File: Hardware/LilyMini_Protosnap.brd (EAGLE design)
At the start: 77.5 x 53.3 mm, 77 parts, among them Q1 ZXMP6A13F, U1 SAMD11D14A-M, U2 AP2112K-3.3V, U3 ALS-PT19, Y1 32.768kHz

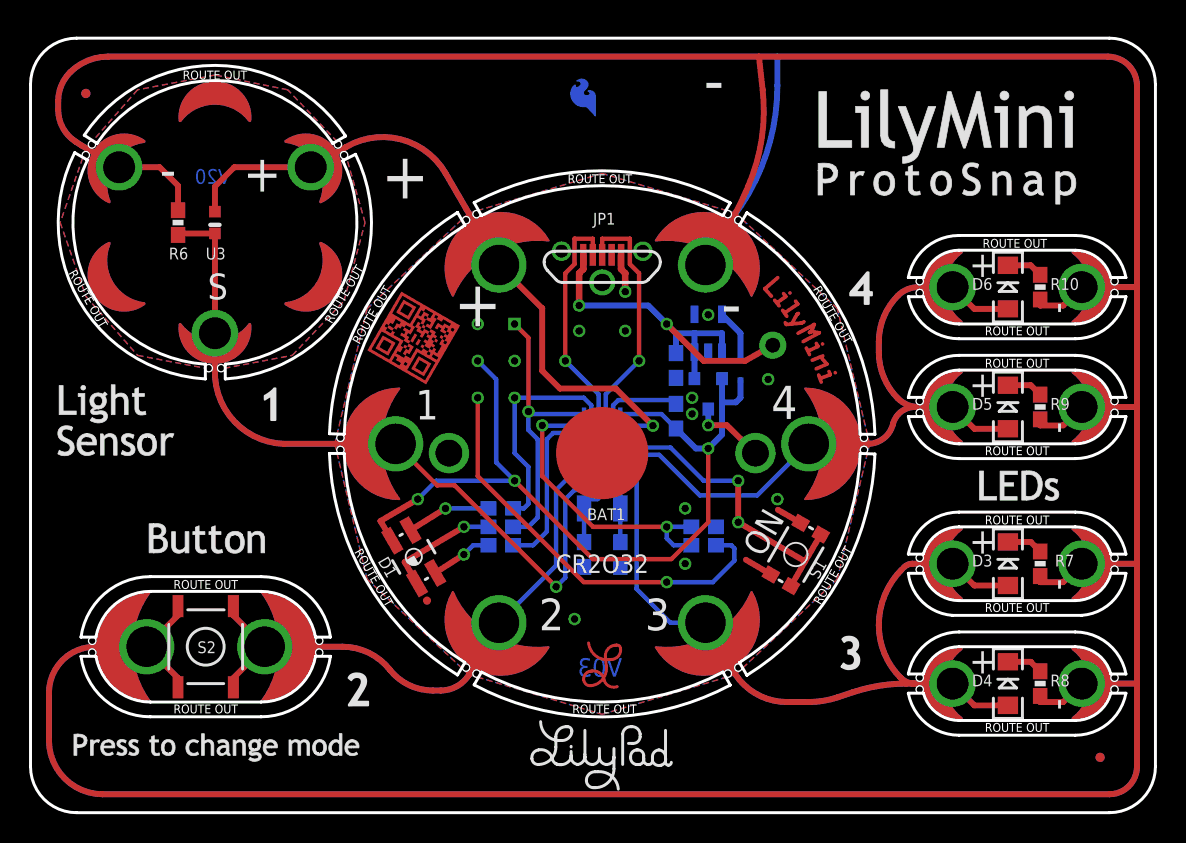
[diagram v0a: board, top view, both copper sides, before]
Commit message: Changed mouse bites from 0.02 to 0.015
Per Advanced Circuits, annular around original 0.02 drill hits would
reduce trace to hairline. Drills reduced to 0.015 to reduce this issue.
Smaller drills may make snapping harder, evaluate on proto.
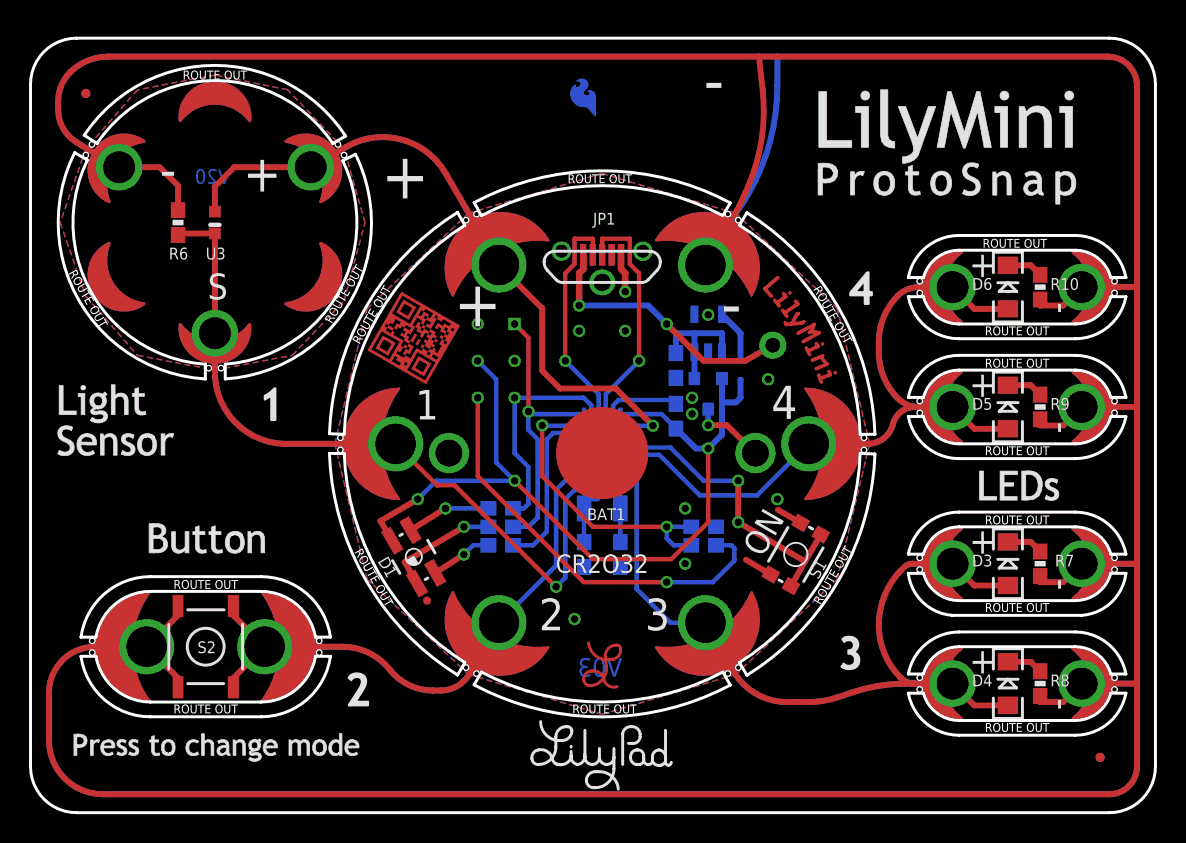
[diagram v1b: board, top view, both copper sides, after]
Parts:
- JP1: value USB_MICROB_PLUGUSB-B-MICRO-SMD-VERT -> (none)
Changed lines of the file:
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@@
 <setting verticaltext="up"/>
 </settings>
-<grid distance="0.25" unitdist="mm" unit="mm" style="lines" multiple="4" display="yes" altdistance="0.00625" altunitdist="inch" altunit="inch"/>
+<grid distance="0.0125" unitdist="inch" unit="inch" style="lines" multiple="4" display="yes" altdistance="0.00625" altunitdist="inch" altunit="inch"/>
 <layers>
 <layer number="1" name="Top" color="4" fill="1" visible="no" active="yes"/>
@@
 <layer number="42" name="bRestrict" color="1" fill="10" visible="no" active="yes"/>
 <layer number="43" name="vRestrict" color="2" fill="10" visible="no" active="yes"/>
-<layer number="44" name="Drills" color="7" fill="1" visible="no" active="yes"/>
-<layer number="45" name="Holes" color="7" fill="1" visible="no" active="yes"/>
+<layer number="44" name="Drills" color="7" fill="1" visible="yes" active="yes"/>
+<layer number="45" name="Holes" color="7" fill="1" visible="yes" active="yes"/>
 <layer number="46" name="Milling" color="3" fill="1" visible="no" active="yes"/>
 <layer number="47" name="Measures" color="7" fill="1" visible="yes" active="yes"/>
@@
 <vertex x="7.3715875" y="31.496"/>
 </polygon>
-<hole x="13.123915625" y="30.615959375" drill="0.508"/>
-<hole x="12.276084375" y="30.615959375" drill="0.508"/>
-<hole x="21.169115625" y="46.019140625" drill="0.508"/>
-<hole x="21.59303125" y="45.284896875" drill="0.508"/>
-<hole x="3.80696875" y="45.284896875" drill="0.508"/>
-<hole x="4.230884375" y="46.019140625" drill="0.508"/>
-<hole x="57.399203125" y="25.81594375" drill="0.508"/>
-<hole x="57.399203125" y="24.98405625" drill="0.508"/>
-<hole x="48.024384375" y="41.22171875" drill="0.508"/>
-<hole x="48.74481875" y="40.805775" drill="0.508"/>
-<hole x="29.99518125" y="40.805775" drill="0.508"/>
-<hole x="30.715615625" y="41.22171875" drill="0.508"/>
-<hole x="21.340796875" y="24.98405625" drill="0.508"/>
-<hole x="21.340796875" y="25.81594375" drill="0.508"/>
-<hole x="30.715615625" y="9.57828125" drill="0.508"/>
-<hole x="29.99518125" y="9.994225" drill="0.508"/>
-<hole x="48.74481875" y="9.994225" drill="0.508"/>
-<hole x="48.024384375" y="9.57828125" drill="0.508"/>
-<hole x="4.248671875" y="11.0236" drill="0.508"/>
-<hole x="4.248671875" y="11.8364" drill="0.508"/>
-<hole x="19.881328125" y="11.0236" drill="0.508"/>
-<hole x="19.881328125" y="11.8364" drill="0.508"/>
-<hole x="61.237853125" y="35.7886" drill="0.508"/>
-<hole x="61.237853125" y="36.6014" drill="0.508"/>
-<hole x="74.652146875" y="35.7886" drill="0.508"/>
-<hole x="74.652146875" y="36.6014" drill="0.508"/>
-<hole x="61.237853125" y="27.5336" drill="0.508"/>
-<hole x="61.237853125" y="28.3464" drill="0.508"/>
-<hole x="74.652146875" y="27.5336" drill="0.508"/>
-<hole x="74.652146875" y="28.3464" drill="0.508"/>
-<hole x="61.237853125" y="16.7386" drill="0.508"/>
-<hole x="61.237853125" y="17.5514" drill="0.508"/>
-<hole x="74.652146875" y="16.7386" drill="0.508"/>
-<hole x="74.652146875" y="17.5514" drill="0.508"/>
-<hole x="61.237853125" y="8.4836" drill="0.508"/>
-<hole x="61.237853125" y="9.2964" drill="0.508"/>
-<hole x="74.652146875" y="8.4836" drill="0.508"/>
-<hole x="74.652146875" y="9.2964" drill="0.508"/>
+<hole x="13.123915625" y="30.615959375" drill="0.381"/>
+<hole x="12.276084375" y="30.615959375" drill="0.381"/>
+<hole x="21.169115625" y="46.019140625" drill="0.381"/>
+<hole x="21.59303125" y="45.284896875" drill="0.381"/>
+<hole x="3.80696875" y="45.284896875" drill="0.381"/>
+<hole x="4.230884375" y="46.019140625" drill="0.381"/>
+<hole x="57.399203125" y="25.81594375" drill="0.381"/>
+<hole x="57.399203125" y="24.98405625" drill="0.381"/>
+<hole x="48.024384375" y="41.22171875" drill="0.381"/>
+<hole x="48.74481875" y="40.805775" drill="0.381"/>
+<hole x="29.99518125" y="40.805775" drill="0.381"/>
+<hole x="30.715615625" y="41.22171875" drill="0.381"/>
+<hole x="21.340796875" y="24.98405625" drill="0.381"/>
+<hole x="21.340796875" y="25.81594375" drill="0.381"/>
+<hole x="30.715615625" y="9.57828125" drill="0.381"/>
+<hole x="29.99518125" y="9.994225" drill="0.381"/>
+<hole x="48.74481875" y="9.994225" drill="0.381"/>
+<hole x="48.024384375" y="9.57828125" drill="0.381"/>
+<hole x="4.248671875" y="11.0236" drill="0.381"/>
+<hole x="4.248671875" y="11.8364" drill="0.381"/>
+<hole x="19.881328125" y="11.0236" drill="0.381"/>
+<hole x="19.881328125" y="11.8364" drill="0.381"/>
+<hole x="61.237853125" y="35.7886" drill="0.381"/>
+<hole x="61.237853125" y="36.6014" drill="0.381"/>
+<hole x="74.652146875" y="35.7886" drill="0.381"/>
+<hole x="74.652146875" y="36.6014" drill="0.381"/>
+<hole x="61.237853125" y="27.5336" drill="0.381"/>
+<hole x="61.237853125" y="28.3464" drill="0.381"/>
+<hole x="74.652146875" y="27.5336" drill="0.381"/>
+<hole x="74.652146875" y="28.3464" drill="0.381"/>
+<hole x="61.237853125" y="16.7386" drill="0.381"/>
+<hole x="61.237853125" y="17.5514" drill="0.381"/>
+<hole x="74.652146875" y="16.7386" drill="0.381"/>
+<hole x="74.652146875" y="17.5514" drill="0.381"/>
+<hole x="61.237853125" y="8.4836" drill="0.381"/>
+<hole x="61.237853125" y="9.2964" drill="0.381"/>
+<hole x="74.652146875" y="8.4836" drill="0.381"/>
+<hole x="74.652146875" y="9.2964" drill="0.381"/>
 <wire x1="1.905" y1="48.887359375" x2="2.808428125" y2="51.068428125" width="0.4064" layer="29" curve="-45"/>
 <wire x1="2.808428125" y1="51.068428125" x2="5.226434375" y2="52.07" width="0.4064" layer="29" curve="-45"/>
@@
 <elements>
 <element name="FRAME1" library="SparkFun-Aesthetics" package="CREATIVE_COMMONS" value="FRAME-LETTER" x="4.445" y="-17.78"/>
-<element name="JP1" library="mike-temp" package="USB-B-MICRO-SMD_VERT" value="USB_MICROB_PLUGUSB-B-MICRO-SMD-VERT" x="39.37" y="38.4175" smashed="yes">
+<element name="JP1" library="mike-temp" package="USB-B-MICRO-SMD_VERT" value="" x="39.37" y="38.4175" smashed="yes">
 <attribute name="NAME" x="40.275" y="40.4975" size="0.8128" layer="25" align="bottom-right"/>
 <attribute name="VALUE" x="40.37" y="35.4175" size="0.4064" layer="27"/>

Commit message: Minor changes pre review
Enlarged copper on programming pins
Added VBATT3 test point
Added TDOCU text for test points
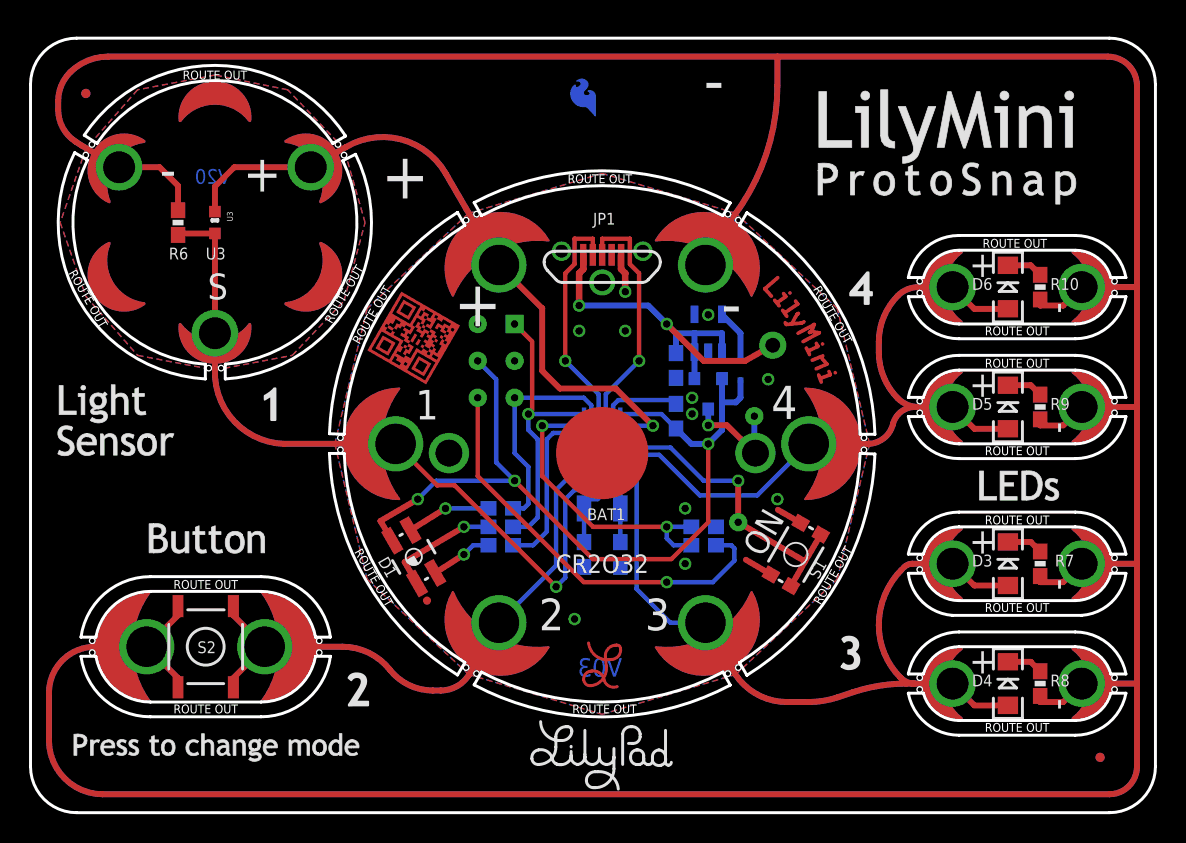
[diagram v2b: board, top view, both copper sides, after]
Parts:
- added JP10: (no value), mike-temp:1X01_POGOPIN_PAD_NOSILK_1SIDE_ROUND
- U3: device mike-temp:ALS-PT19 -> SparkFun-Sensors:ALS-PT19
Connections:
- net BATT3V: now also JP10.P$1
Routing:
- net BATT3V: track 5.14 -> 7.71 mm
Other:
- board text added: "BATT3V"
- board text added: "BLUE/SWDIO"
- board text added: "GND"
- board text added: "NC"
- board text added: "RED/SWDCLK"
- board text added: "RST"
- board text added: "VDD"
- board text added: "White"
- board text removed: "white"

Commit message: Minor updates
Larger fiducials
Sep version numbers on snap (1), LilyMini (1), light (2 - layout and
part change from current)
Added perforations
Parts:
- FD1, FD2, FD3, FD4: value FIDUCIALUFIDUCIAL -> FIDUCIAL1X2; device SparkFun-Aesthetics:MICRO-FIDUCIAL -> SparkFun-Aesthetics:FIDUCIAL-1X2
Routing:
- net GND: vias 11 -> 13
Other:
- board text added: "V1"
- board text added: "V10"
- board text removed: "V03"

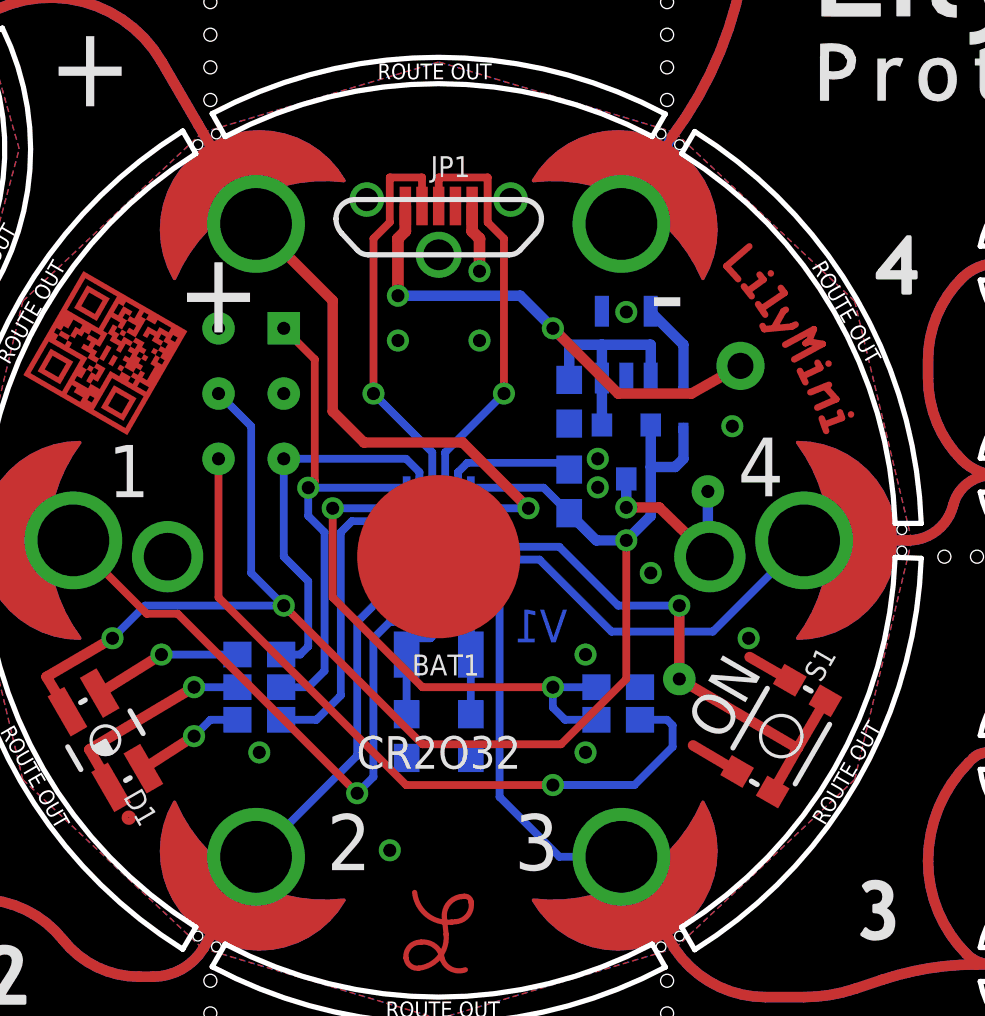
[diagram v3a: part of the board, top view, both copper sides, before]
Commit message: Changes per red review
LED resistors to 150 ohm
VBAT3V test point moved for selective solder
USB P/N lines moved to rear of board for clearance and impedance control
Perforations
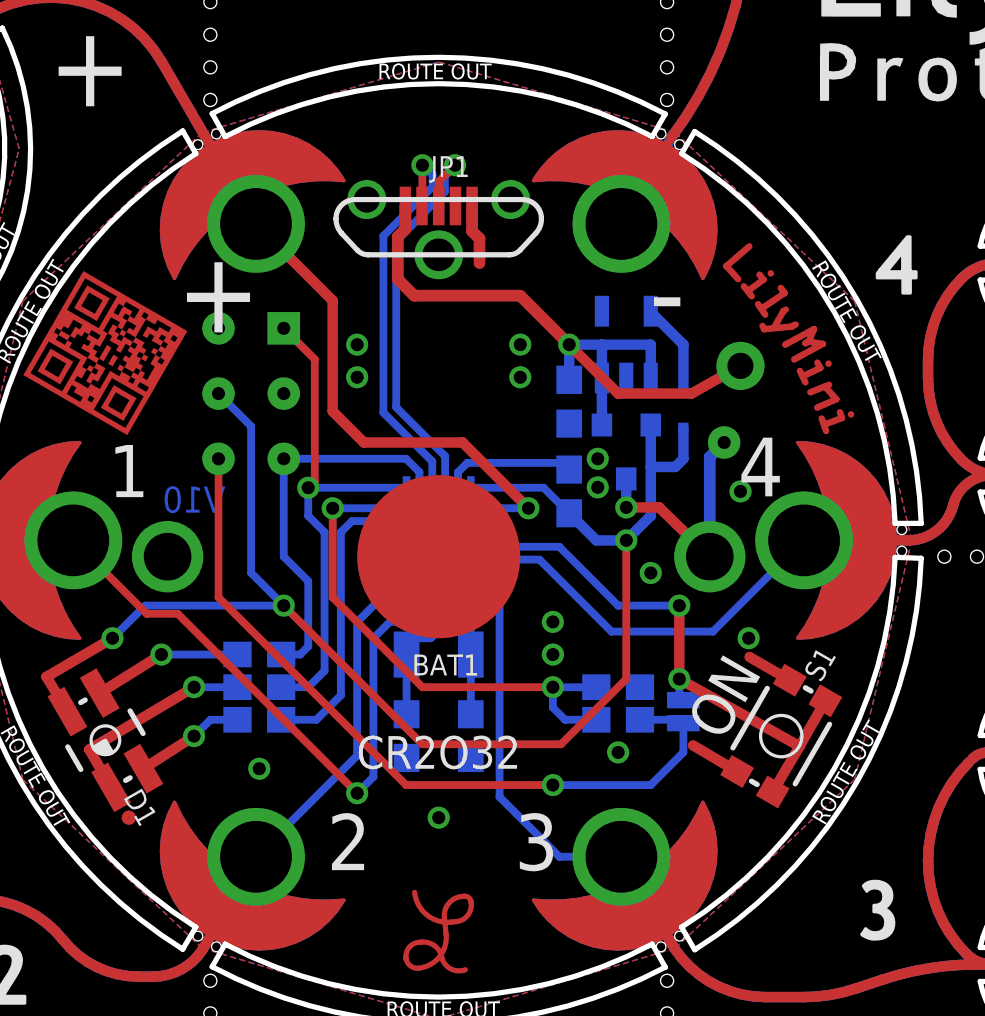
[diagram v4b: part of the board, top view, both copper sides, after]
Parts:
- removed JP10: (no value), mike-temp:1X01_POGOPIN_PAD_NOSILK_1SIDE_ROUND
- added SJ1: (no value), SparkFun-Passives:PAD-JUMPER-2-NO_NO_SILK
- JP3: device mike-temp:1X01_POGOPIN_PAD_NOSILK_1SIDE_ROUND -> mike-temp:1X01_POGOPIN_PAD_NOSILK_1SIDE_SQUARE
- JP4: device mike-temp:1X01_POGOPIN_PAD_NOSILK_1SIDE_SQUARE -> mike-temp:1X01_POGOPIN_PAD_NOSILK_1SIDE_ROUND
- R10, R7, R8, R9: value 100 -> 150
- moved JP3 20.6 mm to (33.3, 33.7), turned to 0 degrees
- moved JP9 19.7 mm to (50.5, 29.2)
- moved JP5 3.59 mm to (33.3, 31.1)
- moved JP7 3.59 mm to (33.3, 28.6)
- moved JP4 2.54 mm to (30.8, 33.7)
- moved JP6 2.54 mm to (30.8, 31.1)
- moved JP8 2.54 mm to (30.8, 28.6)
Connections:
- net USB+ renamed USB_P
- net USB- renamed USB_N
- net !BLUE!/SWDIO: now also JP7.P$1; no longer JP8.P$1
- net !RED!/SWDCLK: now also JP3.P$1; no longer JP4.P$1
- net !RST!: now also JP8.P$1, SJ1.2; no longer JP9.P$1
- net BATT3V: now also JP9.P$1; no longer JP10.P$1
- net BUTTON: now also SJ1.1; no longer JP3.P$1
- net GND: now also JP4.P$1; no longer JP5.P$1
- net VDD: now also JP6.P$1; no longer JP7.P$1
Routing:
- net BATT3V: track 7.71 -> 9.82 mm
- net !RST!: track 28.9 -> 30.2 mm
- net USB5V: track 28.7 -> 27.4 mm, vias 2 -> 1
- net BUTTON: track 20.6 -> 21.6 mm, vias 1 -> 2
- net GND: track 289.8 -> 289.5 mm, vias 13 -> 14
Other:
- board text removed: "V1"

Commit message: Minor changes per checklist
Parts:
- moved FD3 69.8 mm to (73.7, 49.5)
- moved FD4 69.8 mm to (3.81, 3.81)
